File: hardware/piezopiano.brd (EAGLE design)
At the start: 90 x 99.8 mm, 58 parts, among them J1 CON2, Q1 DMN3404L, Q100 DMP3099L, Q2 DMN3404L, Q3 DMN3404L, Q4 DMN3404L, Q5 DMN3404L, Q6 DMN3404L, Q7 DMN3404L, Q8 DMN3404L, U1 MEGA48A-AU, U100 AP7381-50Y-13

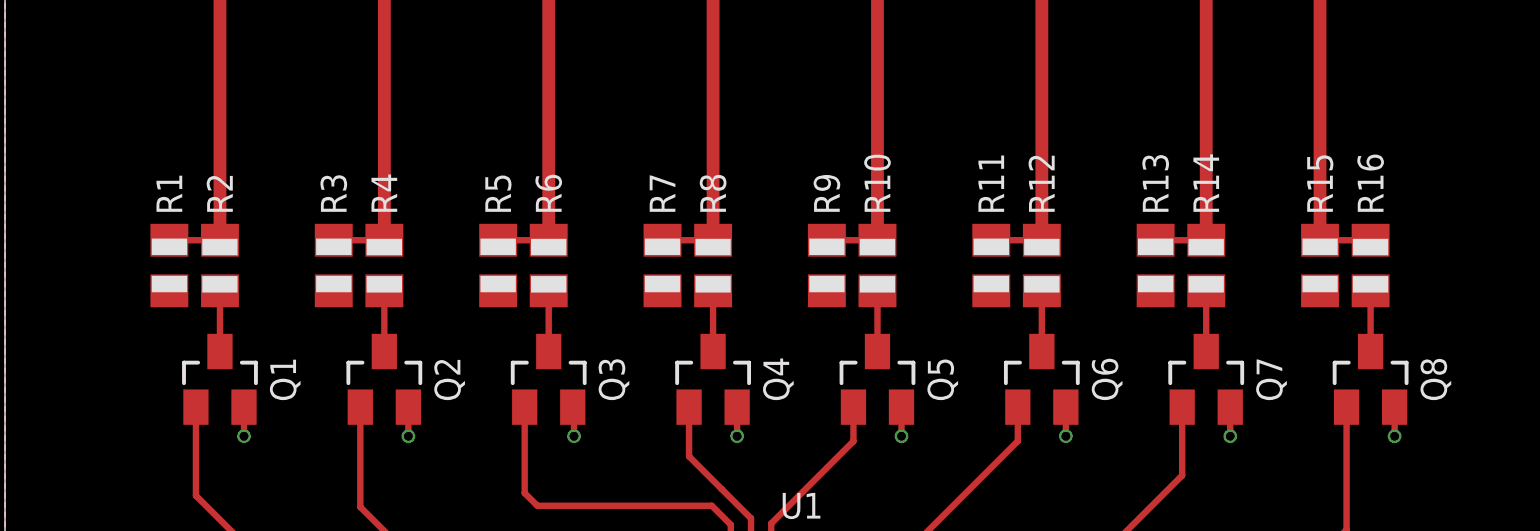
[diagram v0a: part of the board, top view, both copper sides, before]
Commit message: Improved 3D piezo model
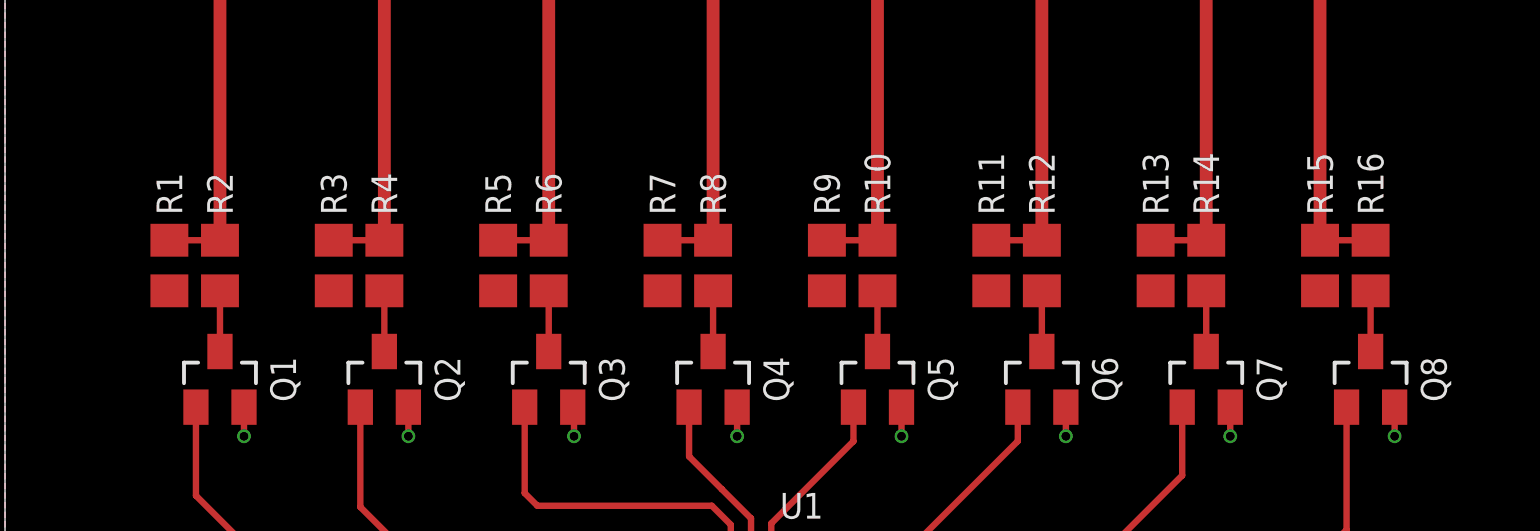
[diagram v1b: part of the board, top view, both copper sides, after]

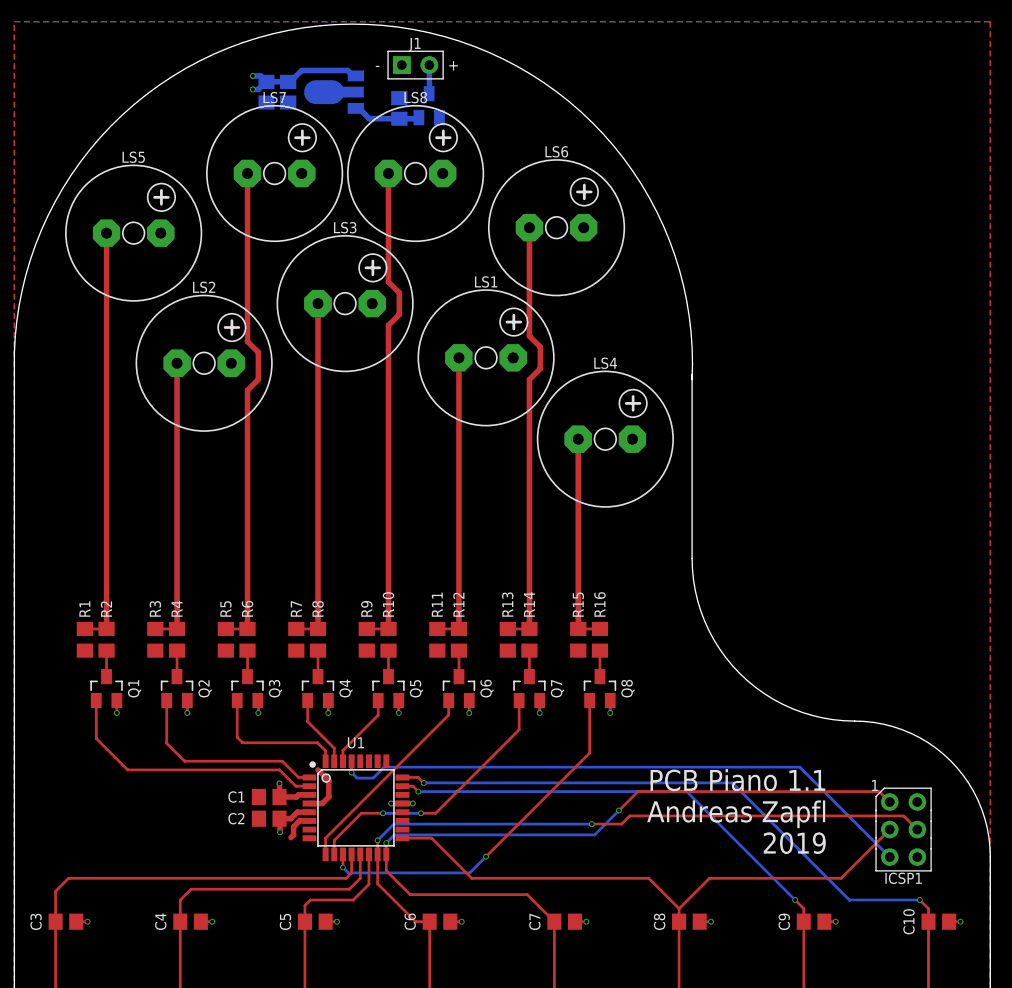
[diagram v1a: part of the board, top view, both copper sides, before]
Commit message: Added USB C and UART
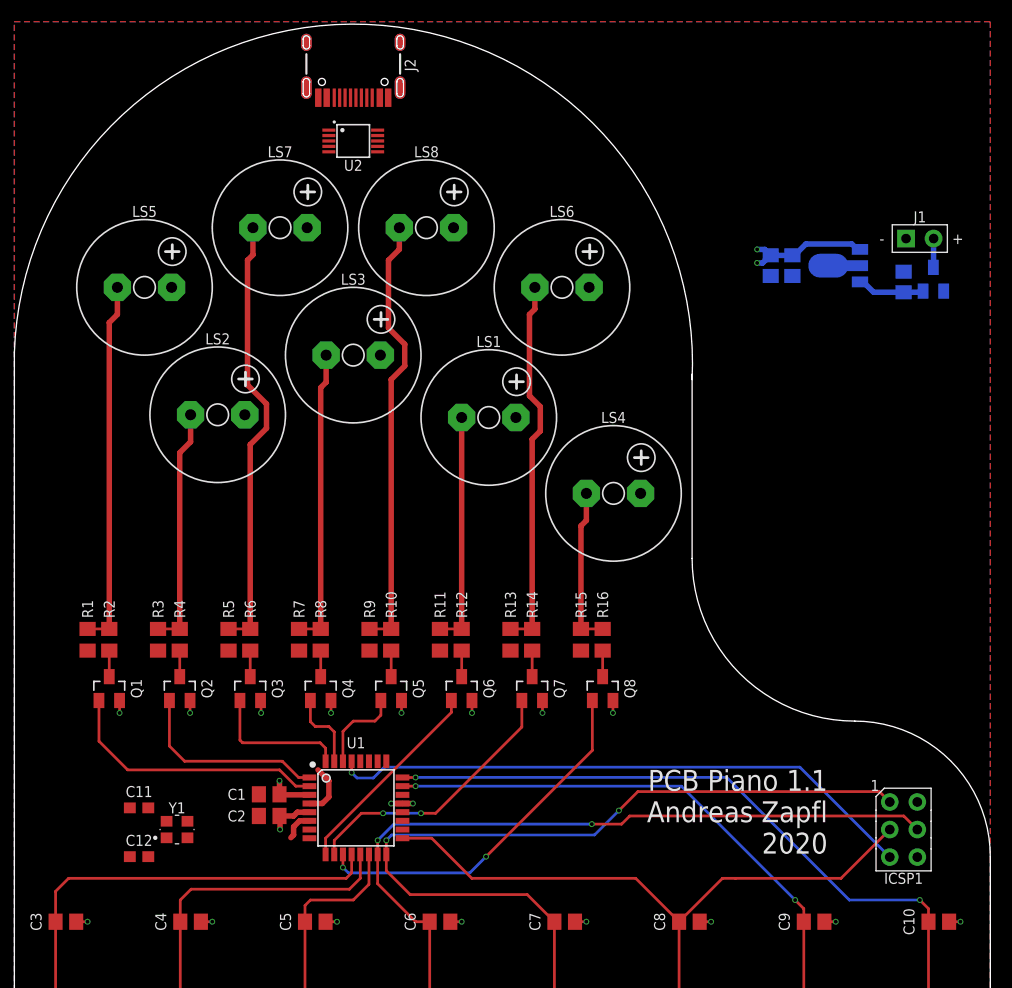
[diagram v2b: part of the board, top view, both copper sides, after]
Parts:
- added C11, C12: 12p, zaan-Capacitors:C0603
- added J2: (no value), zaan-Connectors:USB-C-16P
- added U2: CH340E_MSOP10, zaan-IC-General:MSOP10
- added Y1: 830069392, zaan-Electromechanical:WE-XTAL_CFPX-218
- moved C100 49.2 mm to (82.0, 76.0)
- moved C101 49.2 mm to (69.8, 77.5)
- moved C102 49.2 mm to (71.8, 77.5)
- moved J1 49.2 mm to (83.5, 80.0)
- moved Q100 49.2 mm to (84.8, 76.2)
- moved U100 49.2 mm to (76.0, 77.5)
- moved LS6 5.52 mm to (50.5, 75.5)
- moved LS1 5.51 mm to (43.8, 63.5)
- moved LS5 5.10 mm to (12.0, 75.5)
- moved LS8 5.10 mm to (38.0, 81.0)
- moved LS4 5.06 mm to (55.2, 56.5)
- moved LS7 5.02 mm to (24.5, 81.0)
- moved LS2 4.91 mm to (18.8, 63.8)
- moved LS3 4.81 mm to (31.2, 69.2)
- moved C1 0.25 mm to (23.5, 28.8)
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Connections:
- new net CC1: J2.A5
- new net CC2: J2.B5
- new net D+: J2.A6, J2.B6, U2.1
- new net D-: J2.A7, J2.B7, U2.2
- new net N$19: U2.7
- new net N$20: U2.3
- new net VBUS: J2.VBUS1, J2.VBUS2
- net GND: now also J2.GND, J2.GND2, J2.SHLD1, J2.SHLD2, J2.SHLD3, J2.SHLD4, J2.SHLD5, J2.SHLD6, J2.SHLD7, J2.SHLD8
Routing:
- net N$6: track 27.0 -> 21.5 mm
- net N$16: track 39.8 -> 34.4 mm
- net N$15: track 19.5 -> 14.7 mm
- net N$11: track 38.5 -> 33.8 mm
- net N$10: track 32.0 -> 27.5 mm
- net N$4: track 26.5 -> 22.2 mm
- net N$18: track 44.8 -> 40.6 mm
- net N$13: track 44.8 -> 40.6 mm
- net NOTE5: track 6.95 -> 8.23 mm
- net NOTE2: track 6.62 -> 7.25 mm
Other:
- board text added: "PCB Piano 1.1 Andreas Zapfl 2020"
- board text removed: "PCB Piano 1.1 Andreas Zapfl 2019"

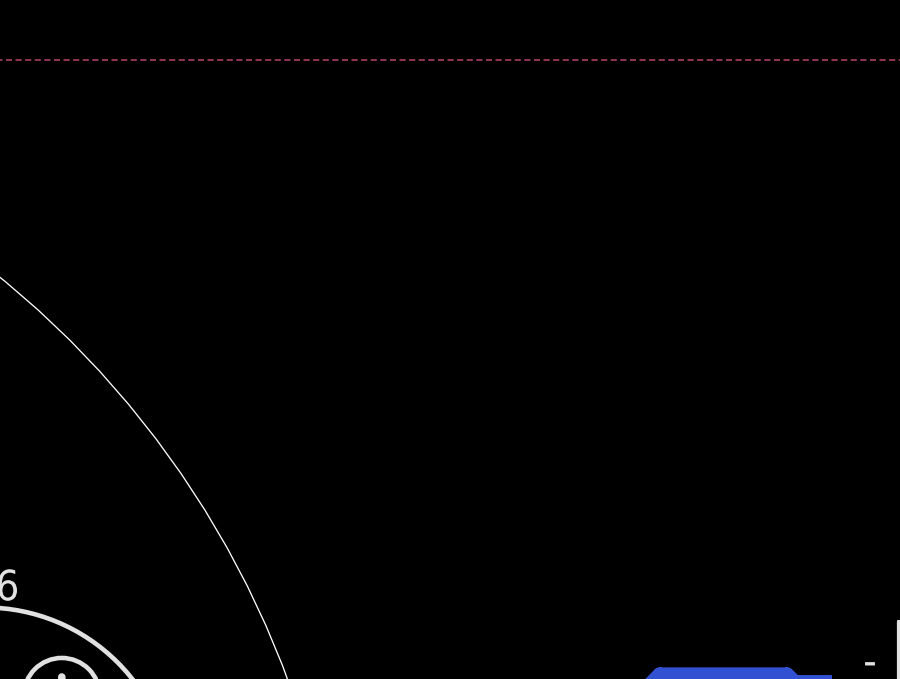
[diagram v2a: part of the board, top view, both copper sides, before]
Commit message: Added Battery Connector
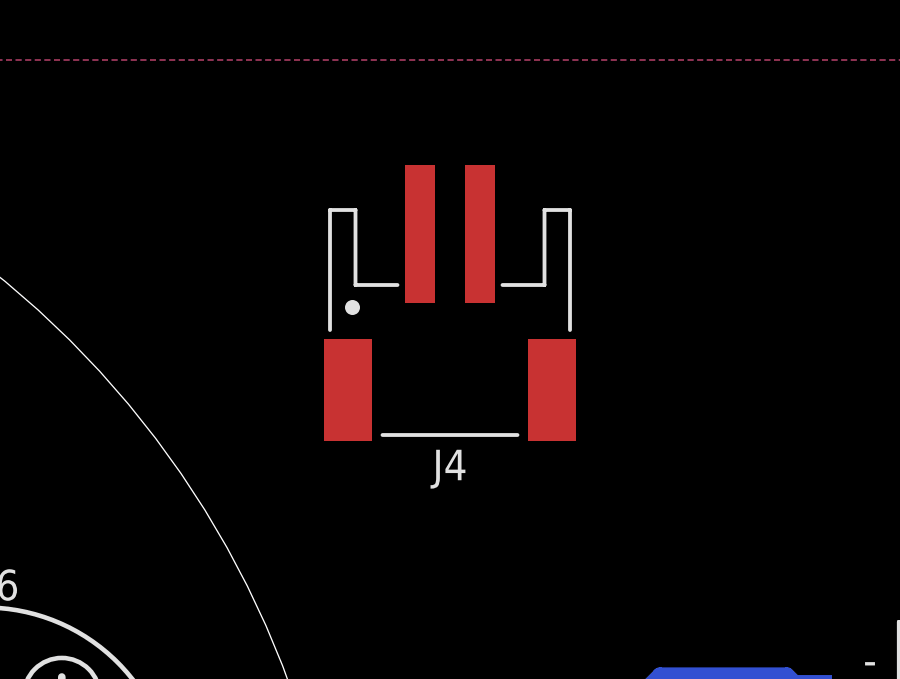
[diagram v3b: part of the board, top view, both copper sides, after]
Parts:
- added J4: JST-PH-2-SMT-SE, zaan-Connectors:JST-PH-2-SMT-SE
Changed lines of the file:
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@@
 <attribute name="VOLTAGE" value="50V" x="11.5" y="23" size="1.778" layer="27" display="off"/>
+</element>
+<element name="J4" library="zaan-Connectors" library_urn="urn:adsk.eagle:library:16759010" package="JST-PH-2-SMT-SE" package3d_urn="urn:adsk.eagle:package:16759071/1" value="JST-PH-2-SMT-SE" x="66" y="90.5" smashed="yes" rot="R180">
+<attribute name="DESCRIPTION" value="JST-PH Header" x="66" y="90.5" size="1.778" layer="27" rot="R180" display="off"/>
+<attribute name="MF" value="JST" x="66" y="90.5" size="1.778" layer="27" rot="R180" display="off"/>
+<attribute name="MPN" value="S2B-PH-SM4-TB(LF)(SN)" x="66" y="90.5" size="1.778" layer="27" rot="R180" display="off"/>
+<attribute name="NAME" x="66" y="86.5" size="1.016" layer="25" font="vector" ratio="15" rot="R180" align="center"/>
+<attribute name="PITCH" value="2.0" x="66" y="90.5" size="1.778" layer="27" rot="R180" display="off"/>
+<attribute name="POSITIONS" value="2" x="66" y="90.5" size="1.778" layer="27" rot="R180" display="off"/>
+<attribute name="VALUE" x="66" y="97.5" size="1.016" layer="27" font="vector" ratio="15" rot="R180" align="center"/>
 </element>
 </elements>

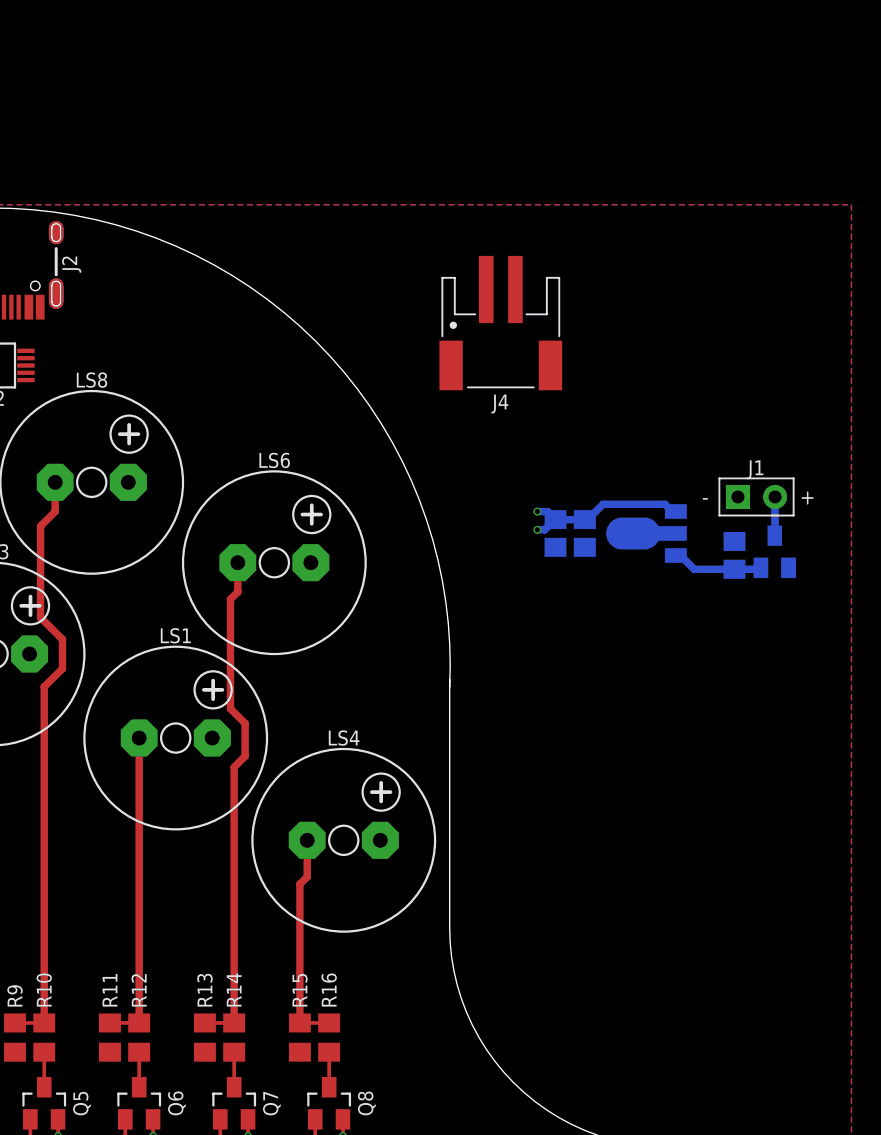
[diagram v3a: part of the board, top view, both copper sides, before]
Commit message: Added Battery Management IC
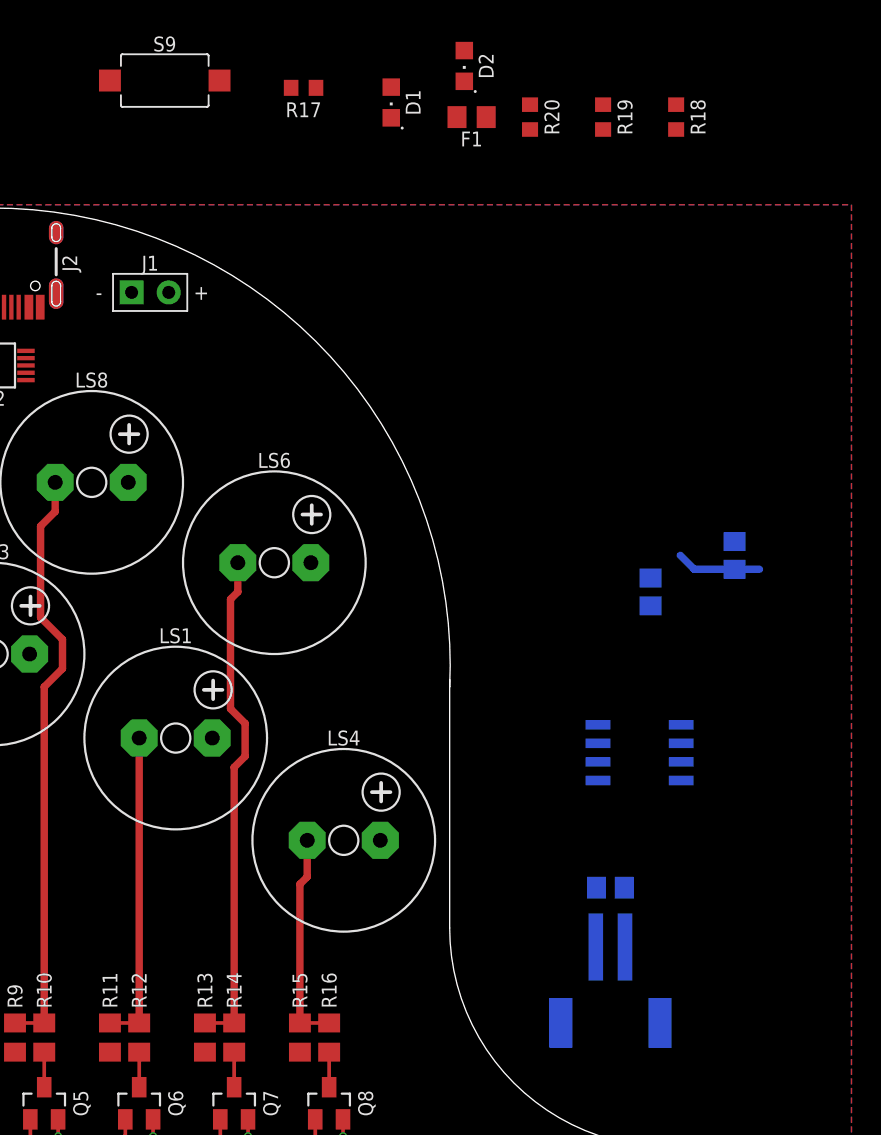
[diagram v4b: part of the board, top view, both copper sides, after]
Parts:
- removed Q100: DMP3099L, zaan-Discrete:SOT23
- removed U100: AP7381-50Y-13, zaan-IC-Power:SOT89
- added D1, D2: LTST-C171KSKT, zaan-Optoelectronics:CHIPLED_0805
- added F1: MF-PSMF035X-2, zaan-Fuses:F0805
- added R17: 10k, zaan-Resistors:R0603
- added R18, R19: 5.1k, zaan-Resistors:R0603
- added R20: 0R, zaan-Resistors:R0603
- added S9: TS-1101-C-W, zaan-Electromechanical:SPST-6X3.6
- added U3: TP4333, zaan-IC-Power:SO8
- moved J4 45.6 mm to (73.5, 45.5), flipped to the bottom
- moved J1 43.8 mm to (42.0, 94.0)
- moved C101 24.5 mm to (73.5, 53.2), turned to 180 degrees
- moved C102 6.02 mm to (76.2, 73.5)
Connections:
- removed net N$19: U2.7
- removed net N$20: U2.3
- new net N$21: C101.1, J4.2, U3.2
- new net N$22: U3.3
- new net N$23: R17.1, U3.5
- new net N$24: R17.2, S9.1
- new net N$25: D1.A, U3.8
- new net N$26: D2.A, U3.7
- net +5V: now also F1.2, R20.2, U2.7, U3.1; no longer C101.1, C102.1, U100.1
- net GND: now also D1.C, D2.C, J4.1, S9.2, U2.3, U3.4; no longer Q100.1, U100.2, U100.2@1
- net N$1: no longer Q100.3
- net N$17: now also R20.1, U3.6; no longer Q100.2, U100.3
- net VBUS: now also F1.1
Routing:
- net +5V: track 19.7 -> 7.74 mm, vias 2 -> 0
- net N$1: track 2.66 -> 0.00 mm
